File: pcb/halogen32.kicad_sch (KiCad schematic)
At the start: 37 parts, among them J1 Conn_02x05_Odd_Even, J2 USB_C_Receptacle_USB2.0_16P, J3 Conn_01x04_Pin, J4 Conn_01x20_Socket, J5 Conn_01x14_Socket, J6 Barrel_Jack, SW1 SW_SPDT, SW2 SW_SPDT, U1 STM32F411CEUx, U2 AMS1117-3.3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

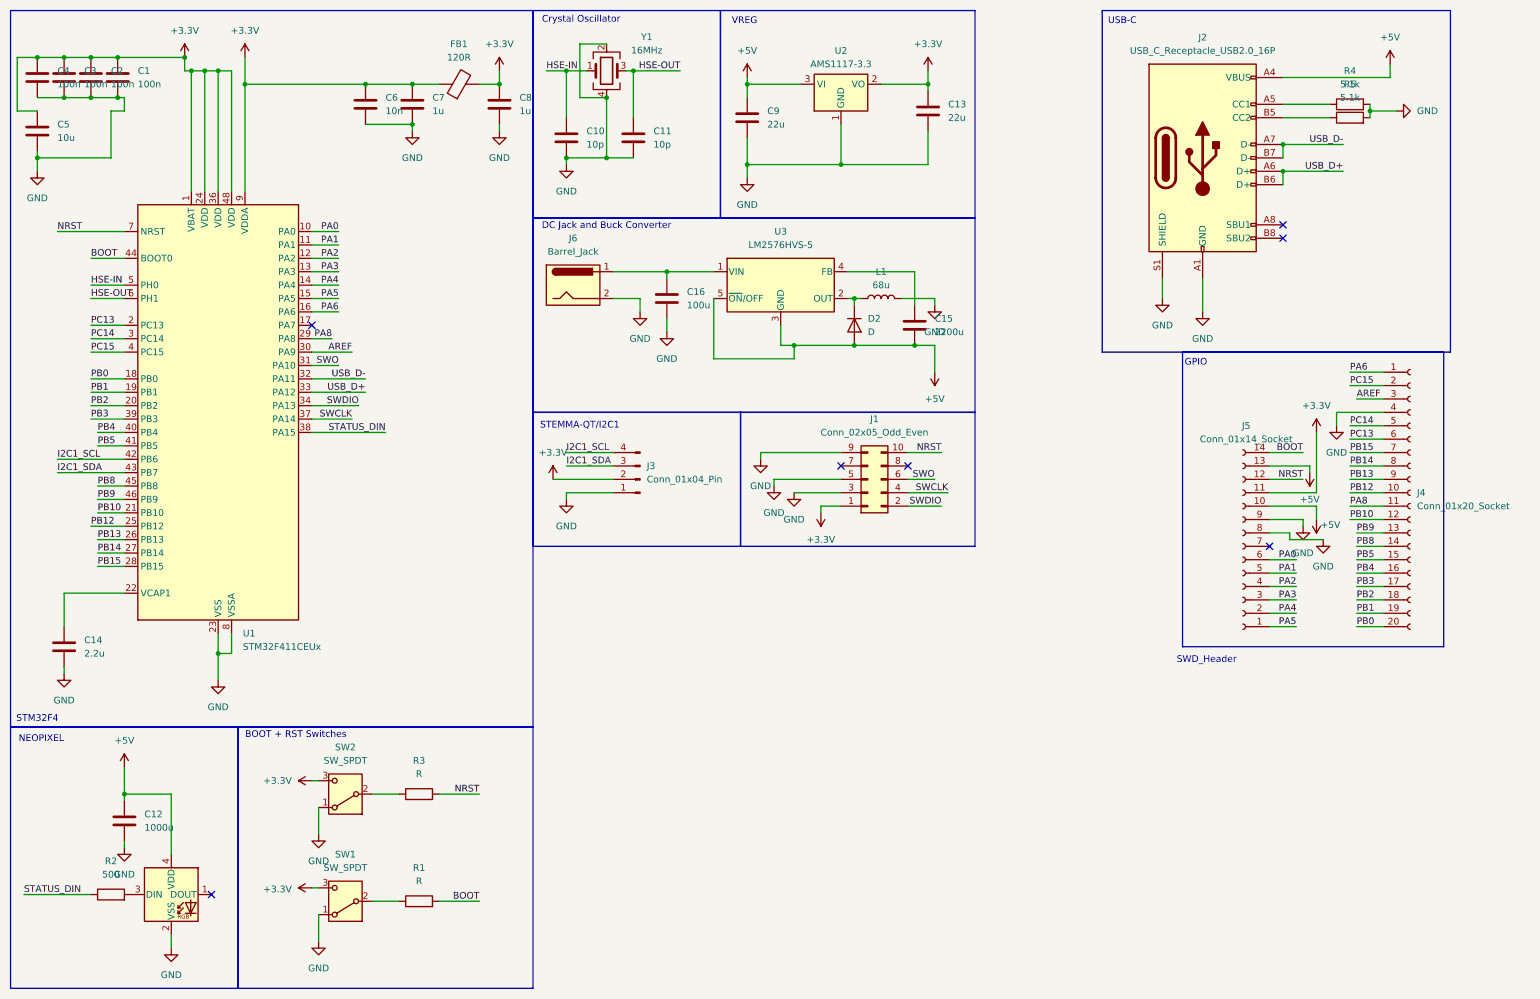
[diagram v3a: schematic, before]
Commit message: Worked on footprints, just need to add SWD header, boot and reset switches, and Crystal footprints.
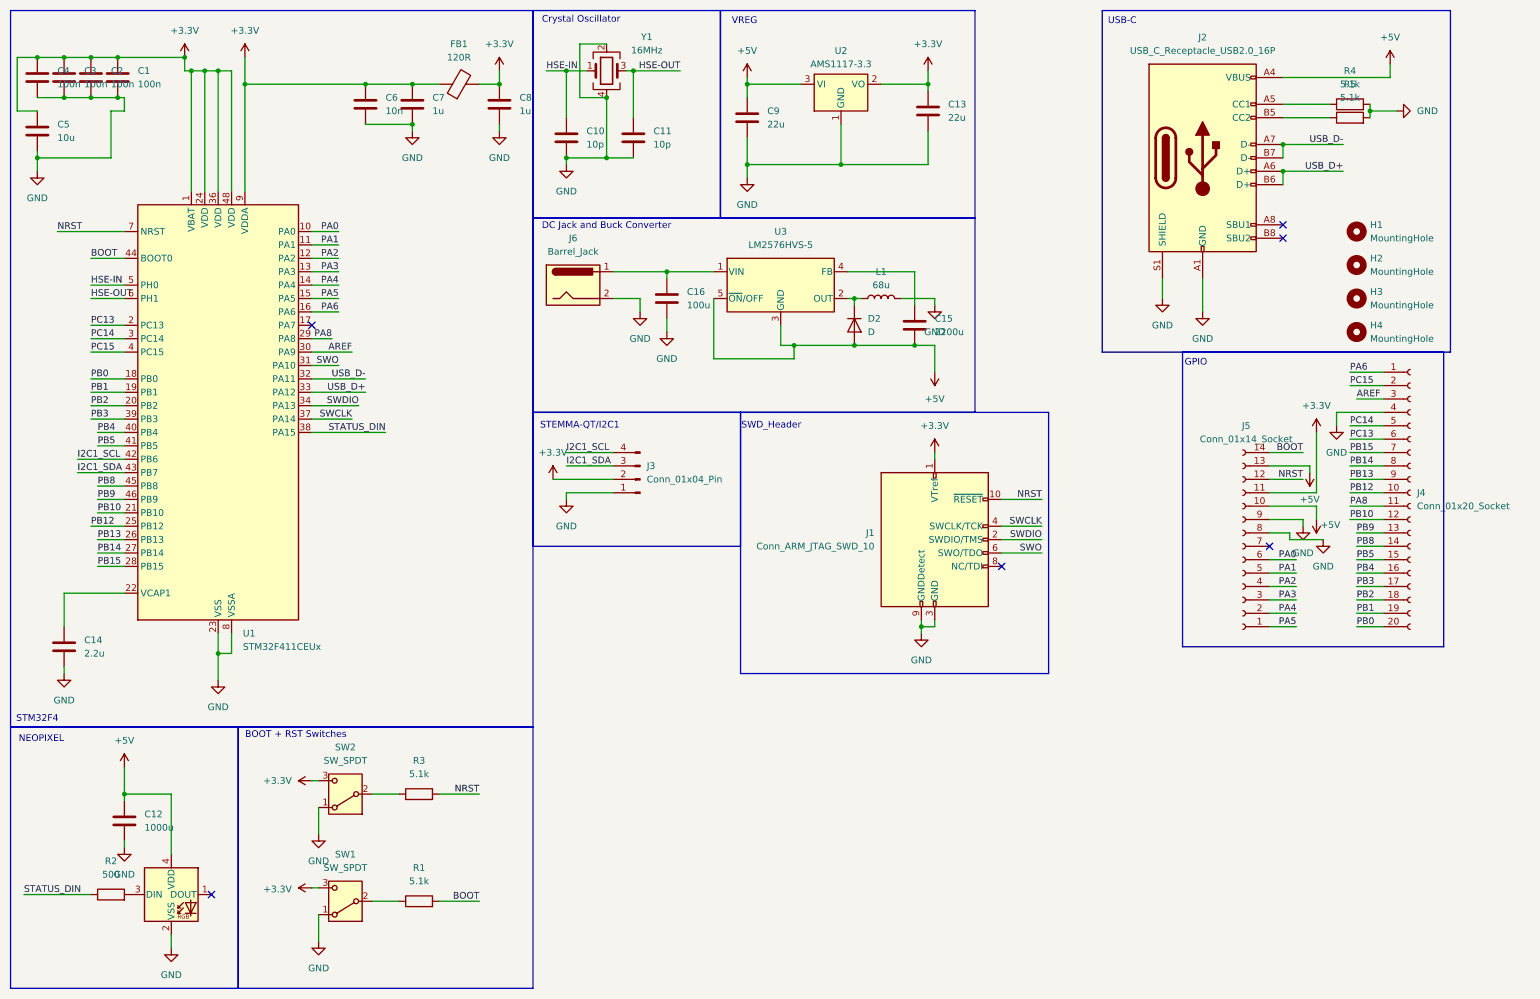
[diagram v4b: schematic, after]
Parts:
- removed J1: Conn_02x05_Odd_Even, symbol Connector_Generic:Conn_02x05_Odd_Even
- added H1, H2, H3, H4: MountingHole, MountingHole:MountingHole_2.5mm, symbol Mechanical:MountingHole
- added J1: Conn_ARM_JTAG_SWD_10, symbol Connector:Conn_ARM_JTAG_SWD_10
- C1, C10, C11, C12, C13, C14, C15, C16, C2, C3, C4, C5, C6, C7, C8, C9: footprint (none) -> Capacitor_SMD:CP_Elec_3x5.3
- D2: footprint (none) -> Diode_SMD:D_0201_0603Metric
- J2: footprint (none) -> Connector_USB:USB_C_Plug_Molex_105444
- J3: footprint (none) -> Connector_JST:JST_EH_B4B-EH-A_1x04_P2.50mm_Vertical
- J4: footprint (none) -> Connector_PinSocket_1.00mm:PinSocket_1x20_P1.00mm_Vertical
- J5: footprint (none) -> Connector_PinSocket_1.00mm:PinSocket_1x14_P1.00mm_Vertical
- J6: footprint (none) -> Connector_BarrelJack:BarrelJack_CLIFF_FC681465S_SMT_Horizontal
- L1: footprint (none) -> Inductor_SMD:L_6.3x6.3_H3
- R1, R3: value R -> 5.1k; footprint (none) -> Resistor_SMD:R_0201_0603Metric
- R2, R4, R5: footprint (none) -> Resistor_SMD:R_0201_0603Metric
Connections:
- net +3.3V: now also J1.1 (VTref)
- net GND: now also J1.3 (GND), J1.5 (GND), J1.9 (GNDDetect)
- net NRST: now also J1.10 (~{RESET})
- net SWCLK: now also J1.4 (SWCLK/TCK)
- net SWDIO: now also J1.2 (SWDIO/TMS)
- net SWO: now also J1.6 (SWO/TDO)
- no-connect marks 7 -> 6

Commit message: Assigned footprints and imported footprints into pcb layout.
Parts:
- FB1: footprint (none) -> Ferrite_THT:LairdTech_28C0236-0JW-10
- J1: footprint (none) -> Connector_PinHeader_1.27mm:PinHeader_2x05_P1.27mm_Vertical
- SW1, SW2: footprint (none) -> Button_Switch_SMD:SW_SPST_TL3342
- Y1: footprint (none) -> Crystal:Crystal_SMD_0603-2Pin_6.0x3.5mm
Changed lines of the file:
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@@
 	)
 	(symbol
+		(lib_id "Connector:Conn_ARM_JTAG_SWD_10")
+		(at 187.96 113.03 0)
+		(unit 1)
+		(exclude_from_sim no)
+		(in_bom yes)
+		(on_board yes)
+		(dnp no)
+		(fields_autoplaced yes)
+		(property "Reference" "J1"
+			(at 176.53 111.7599 0)
+			(effects
+				(font
+					(size 1.27 1.27)
+				)
+				(justify right)
+			)
+		)
+		(property "Value" "Conn_ARM_JTAG_SWD_10"
+			(at 176.53 114.2999 0)
+			(effects
+				(font
+					(size 1.27 1.27)
+				)
+				(justify right)
+			)
+		)
+		(property "Footprint" "Connector_PinHeader_1.27mm:PinHeader_2x05_P1.27mm_Vertical"
+			(at 187.96 113.03 0)
+			(effects
+				(font
+					(size 1.27 1.27)
+				)
+				(hide yes)
+			)
+		)
+		(property "Datasheet" "http://infocenter.arm.com/help/topic/com.arm.doc.ddi0314h/DDI0314H_coresight_components_trm.pdf"
+			(at 179.07 144.78 90)
+			(effects
+				(font
+					(size 1.27 1.27)
+				)
+				(hide yes)
+			)
+		)
+		(property "Description" "Cortex Debug Connector, standard ARM Cortex-M SWD and JTAG interface"
+			(at 187.96 113.03 0)
+			(effects
+				(font
+					(size 1.27 1.27)
+				)
+				(hide yes)
+			)
+		)
+		(pin "3"
+		)
+		(pin "5"
+		)
+		(pin "2"
+		)
+		(pin "1"
+		)
+		(pin "9"
+		)
+		(pin "6"
+		)
+		(pin "4"
+		)
+		(pin "10"
+		)
+		(pin "7"
+		)
+		(pin "8"
+		)
+		(instances
+			(project ""
+				(path "/0dddf3a6-05c9-4d23-8b33-d0c9438795f8"
+					(reference "J1")
+					(unit 1)
+				)
+			)
+		)
+	)
+	(symbol
 		(lib_id "Mechanical:MountingHole")
 		(at 267.97 73.66 0)
@@
 			)
 		)
-		(property "Footprint" ""
+		(property "Footprint" "Button_Switch_SMD:SW_SPST_TL3342"
 			(at 76.2 161.29 0)
 			(effects
@@
 			)
 		)
-		(property "Footprint" ""
+		(property "Footprint" "Button_Switch_SMD:SW_SPST_TL3342"
 			(at 76.2 181.61 0)
 			(effects
@@
 			)
 		)
-		(property "Footprint" ""
+		(property "Footprint" "Crystal:Crystal_SMD_0603-2Pin_6.0x3.5mm"
 			(at 125.73 24.13 0)
 			(effects
@@
 			)
 		)
-		(property "Footprint" ""
+		(property "Footprint" "Ferrite_THT:LairdTech_28C0236-0JW-10"
 			(at 97.79 28.448 90)
 			(effects
@@
 					(unit 1)
 				)
-			)
-		)
-	)
-	(symbol
-		(lib_id "Connector:Conn_ARM_JTAG_SWD_10")
-		(at 187.96 113.03 0)
-		(unit 1)
-		(exclude_from_sim no)
-		(in_bom yes)
-		(on_board yes)
-		(dnp no)
-		(fields_autoplaced yes)
-		(property "Reference" "J1"
-			(at 176.53 111.7599 0)
-			(effects
-				(font
-					(size 1.27 1.27)
-				)
-				(justify right)
-			)
-		)
-		(property "Value" "Conn_ARM_JTAG_SWD_10"
-			(at 176.53 114.2999 0)
-			(effects
-				(font
-					(size 1.27 1.27)
-				)
-				(justify right)
-			)
-		)
-		(property "Footprint" ""
-			(at 187.96 113.03 0)
-			(effects
-				(font
-					(size 1.27 1.27)
-				)
-				(hide yes)
-			)
-		)
-		(property "Datasheet" "http://infocenter.arm.com/help/topic/com.arm.doc.ddi0314h/DDI0314H_coresight_components_trm.pdf"
-			(at 179.07 144.78 90)
-			(effects
-				(font
-					(size 1.27 1.27)
-				)
-				(hide yes)
-			)
-		)
-		(property "Description" "Cortex Debug Connector, standard ARM Cortex-M SWD and JTAG interface"
-			(at 187.96 113.03 0)
-			(effects
-				(font
-					(size 1.27 1.27)
-				)
-				(hide yes)
-			)
-		)
-		(pin "6"
-		)
-		(pin "10"
-		)
-		(pin "5"
-		)
-		(pin "3"
-		)
-		(pin "1"
-		)
-		(pin "7"
-		)
-		(pin "4"
-		)
-		(pin "8"
-		)
-		(pin "2"
-		)
-		(pin "9"
-		)
-		(instances
-			(project ""
-				(path "/0dddf3a6-05c9-4d23-8b33-d0c9438795f8"
-					(reference "J1")
-					(unit 1)
-				)
